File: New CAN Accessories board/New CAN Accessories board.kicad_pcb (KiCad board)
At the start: 2 copper layers, 76 parts, among them J1 39301040, J10 39301060, J2 39301040, J3 39301040, J4 39301040, J5 39301040, J6 39301040, J7 39301040, J8 39301040, J9 39301060, Q1 IRLML6344TRPBF, Q2 IRLML6344TRPBF, Q3 IRLML6344TRPBF, Q4 IRLML6344TRPBF, Q5 IRLML6344TRPBF, Q6 IRLML6344TRPBF, Q7 IRLML6344TRPBF, Q8 IRLML6344TRPBF, SW1 SW_DPDT_x2, SW3 SW_DPDT_x2, U1 NUCLEO_L432KC, U2 MCP2562FD-E_SN

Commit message: preliminary layout complete
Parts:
- removed C1, C2: 100nF, Capacitor_SMD:C_0805_2012Metric
- removed F11: Fuse, footprint:3586KTR
- removed R1, R11, R13, R15, R3, R5, R7, R9: 100, Resistor_SMD:R_0805_2012Metric
- removed R10, R12, R14, R16, R2, R26, R27, R4, R6, R8: 10K, Resistor_SMD:R_0805_2012Metric
- removed R17, R18, R19, R20, R21, R22, R23, R24: 0.05, Resistor_SMD:R_2512_6332Metric_Pad1.40x3.35mm_HandSolder
- removed R25: 120, Resistor_SMD:R_0805_2012Metric
- removed SW1, SW3: SW_DPDT_x2, footprint:SWITCH_011CQN
- removed U2: MCP2562FD-E_SN, footprint:MCP2562FD-E_SN
- added Cop1: 100nF, Capacitor_SMD:C_0805_2012Metric, B.Cu at (27.1, 40.9)
- added Cop2: 100nF, Capacitor_SMD:C_0805_2012Metric, B.Cu at (38.4, 40.9)
- added Cop3: 100nF, Capacitor_SMD:C_0805_2012Metric, B.Cu at (49.7, 40.9)
- added Cop4: 100nF, Capacitor_SMD:C_0805_2012Metric, B.Cu at (61.1, 40.9)
- added Cop5: 100nF, Capacitor_SMD:C_0805_2012Metric, B.Cu at (72.4, 40.9)
- added Cop6: 100nF, Capacitor_SMD:C_0805_2012Metric, B.Cu at (83.8, 40.9)
- added Cop7: 100nF, Capacitor_SMD:C_0805_2012Metric, B.Cu at (95.1, 40.9)
- added Cop8: 100nF, Capacitor_SMD:C_0805_2012Metric, B.Cu at (106.5, 40.9)
- added Ctr1: 100nF, Capacitor_SMD:C_0805_2012Metric, B.Cu at (76.2, 75.3)
- added Ctr2: 100nF, Capacitor_SMD:C_0805_2012Metric, B.Cu at (65.7, 77.6)
- added F8: Fuse, footprint:3586KTR, F.Cu at (105.4, 47.0)
- added J11: ATF13-2P-BM03, footprint:ATF132PBM03, F.Cu at (51.7, 68.5)
- added Rled1: 100, Resistor_SMD:R_0805_2012Metric, F.Cu at (22.9, 56.8)
- added Rled2: 100, Resistor_SMD:R_0805_2012Metric, F.Cu at (34.3, 56.8)
- added Rled3: 100, Resistor_SMD:R_0805_2012Metric, F.Cu at (45.6, 56.8)
- added Rled4: 100, Resistor_SMD:R_0805_2012Metric, F.Cu at (56.9, 56.8)
- added Rled5: 100, Resistor_SMD:R_0805_2012Metric, F.Cu at (68.3, 56.8)
- added Rled6: 100, Resistor_SMD:R_0805_2012Metric, F.Cu at (79.6, 56.8)
- added Rled7: 100, Resistor_SMD:R_0805_2012Metric, F.Cu at (91.0, 56.8)
- added Rled8: 100, Resistor_SMD:R_0805_2012Metric, F.Cu at (102.3, 56.8)
- added Rpd1: 10K, Resistor_SMD:R_0805_2012Metric, F.Cu at (21.6, 53.9)
- added Rpd2: 10K, Resistor_SMD:R_0805_2012Metric, F.Cu at (32.9, 53.9)
- added Rpd3: 10K, Resistor_SMD:R_0805_2012Metric, F.Cu at (44.3, 53.9)
- added Rpd4: 10K, Resistor_SMD:R_0805_2012Metric, F.Cu at (55.6, 53.9)
- added Rpd5: 10K, Resistor_SMD:R_0805_2012Metric, F.Cu at (67.0, 53.9)
- added Rpd6: 10K, Resistor_SMD:R_0805_2012Metric, F.Cu at (78.3, 53.9)
- added Rpd7: 10K, Resistor_SMD:R_0805_2012Metric, F.Cu at (89.7, 53.9)
- added Rpd8: 10K, Resistor_SMD:R_0805_2012Metric, F.Cu at (101.0, 53.9)
- added Rpd9: 10K, Resistor_SMD:R_0805_2012Metric, B.Cu at (69.3, 83.3)
- added Rsh1: 0.05, Resistor_SMD:R_2512_6332Metric_Pad1.40x3.35mm_HandSolder, B.Cu at (22.3, 44.6)
- added Rsh2: 0.05, Resistor_SMD:R_2512_6332Metric_Pad1.40x3.35mm_HandSolder, B.Cu at (33.7, 44.6)
- added Rsh3: 0.05, Resistor_SMD:R_2512_6332Metric_Pad1.40x3.35mm_HandSolder, B.Cu at (45.0, 44.6)
- added Rsh4: 0.05, Resistor_SMD:R_2512_6332Metric_Pad1.40x3.35mm_HandSolder, B.Cu at (56.4, 44.6)
- added Rsh5: 0.05, Resistor_SMD:R_2512_6332Metric_Pad1.40x3.35mm_HandSolder, B.Cu at (67.7, 44.6)
- added Rsh6: 0.05, Resistor_SMD:R_2512_6332Metric_Pad1.40x3.35mm_HandSolder, B.Cu at (79.0, 44.6)
- added Rsh7: 0.05, Resistor_SMD:R_2512_6332Metric_Pad1.40x3.35mm_HandSolder, B.Cu at (90.4, 44.6)
- added Rsh8: 0.05, Resistor_SMD:R_2512_6332Metric_Pad1.40x3.35mm_HandSolder, B.Cu at (101.7, 44.6)
- added Rterm1: 120, Resistor_SMD:R_0805_2012Metric, B.Cu at (29.0, 88.4)
- added SWsel1: SW_DPDT_x2, footprint:SWITCH_011CQN, F.Cu at (72.7, 85.7)
- added T1: MCP2562FD-E_SN, footprint:MCP2562FD-E_SN, B.Cu at (70.5, 74.7)
- J10: value 39301060 -> 39301040; footprint Connector_Molex:Molex_Mini-Fit_Jr_5569-06A2_2x03_P4.20mm_Horizontal -> Connector_Molex:Molex_Mini-Fit_Jr_5569-04A2_2x02_P4.20mm_Horizontal
- JP4, OP1, OP2, OP3, OP4, OP5, OP6, OP7, OP8: moved to B.Cu
- moved JP4 141.3 mm to (33.0, 89.3)
- moved D1 128.8 mm to (20.6, 56.7), turned to 90 degrees
- moved D2 119.2 mm to (32.0, 56.7), turned to 90 degrees
- moved OP1 117.6 mm to (27.1, 44.6), turned to 90 degrees
- moved J10 114.7 mm to (33.0, 84.3), turned to 90 degrees
- moved OP2 110.4 mm to (38.4, 44.6), turned to 90 degrees
- moved D3 110.1 mm to (43.3, 56.7), turned to 90 degrees
- moved OP3 104.1 mm to (49.7, 44.6), turned to 90 degrees
- moved Q1 103.5 mm to (25.7, 56.8), turned to 90 degrees
- moved D4 101.5 mm to (54.7, 56.7), turned to 90 degrees
- moved J9 99.9 mm to (33.0, 73.2), turned to 90 degrees
- moved OP4 99.1 mm to (61.1, 44.6), turned to 90 degrees
- moved Q2 99.0 mm to (37.1, 56.8), turned to 90 degrees
- moved OP5 95.3 mm to (72.4, 44.6), turned to 90 degrees
- moved D5 93.6 mm to (66.0, 56.7), turned to 90 degrees
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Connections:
- net /5V renamed 5V
- J10 pad 1: +12V -> /CANL
- J10 pad 2: +12V -> /CANH
- J10 pad 4: /CANL -> GND
- U1 pad PA10: unconnected-(U1-D0-PadPA10) -> /GATE8
- U1 pad PA11: /CANRX -> /STBY
- U1 pad PA8: /GATE2 -> /GATE3
- U1 pad PA9: /STBY -> /CANRX
- U1 pad PB0: /BOARD_SW -> /GATE7
- U1 pad PB1: /GATE1 -> /GATE4
- U1 pad PB3: /TELEM_SW -> /BOARD_SW
- U1 pad PB4: /GATE6 -> /GATE1
- U1 pad PB5: /GATE5 -> /GATE2
- U1 pad PB6: /GATE4 -> /GATE5
- U1 pad PB7: /GATE3 -> /GATE6
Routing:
- net 5V: track 0.00 -> 197.7 mm, vias 0 -> 3
- net +12V: track 0.00 -> 177.6 mm, vias 0 -> 1
- net /OA8: track 0.00 -> 85.4 mm, vias 0 -> 2
- net /OA1: track 0.00 -> 77.8 mm, vias 0 -> 2
- net /OA7: track 0.00 -> 72.3 mm, vias 0 -> 2
- net /OA2: track 0.00 -> 69.1 mm, vias 0 -> 2
- net /OA6: track 0.00 -> 63.5 mm, vias 0 -> 2
- net /OA3: track 0.00 -> 62.9 mm, vias 0 -> 2
- net /GATE1: track 0.00 -> 58.7 mm
- net /CANH: track 0.00 -> 54.1 mm
- net /OA4: track 0.00 -> 51.9 mm, vias 0 -> 2
- net /OA5: track 0.00 -> 51.1 mm, vias 0 -> 2
- net /GATE2: track 0.00 -> 49.9 mm
- net /CANL: track 0.00 -> 49.2 mm
- net GND: track 0.00 -> 45.4 mm, vias 0 -> 24
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- added copper zone on B.Cu, net +12V
- added copper zone on B.Cu, net GND
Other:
- board outline added: 105.1 x 85.8 mm

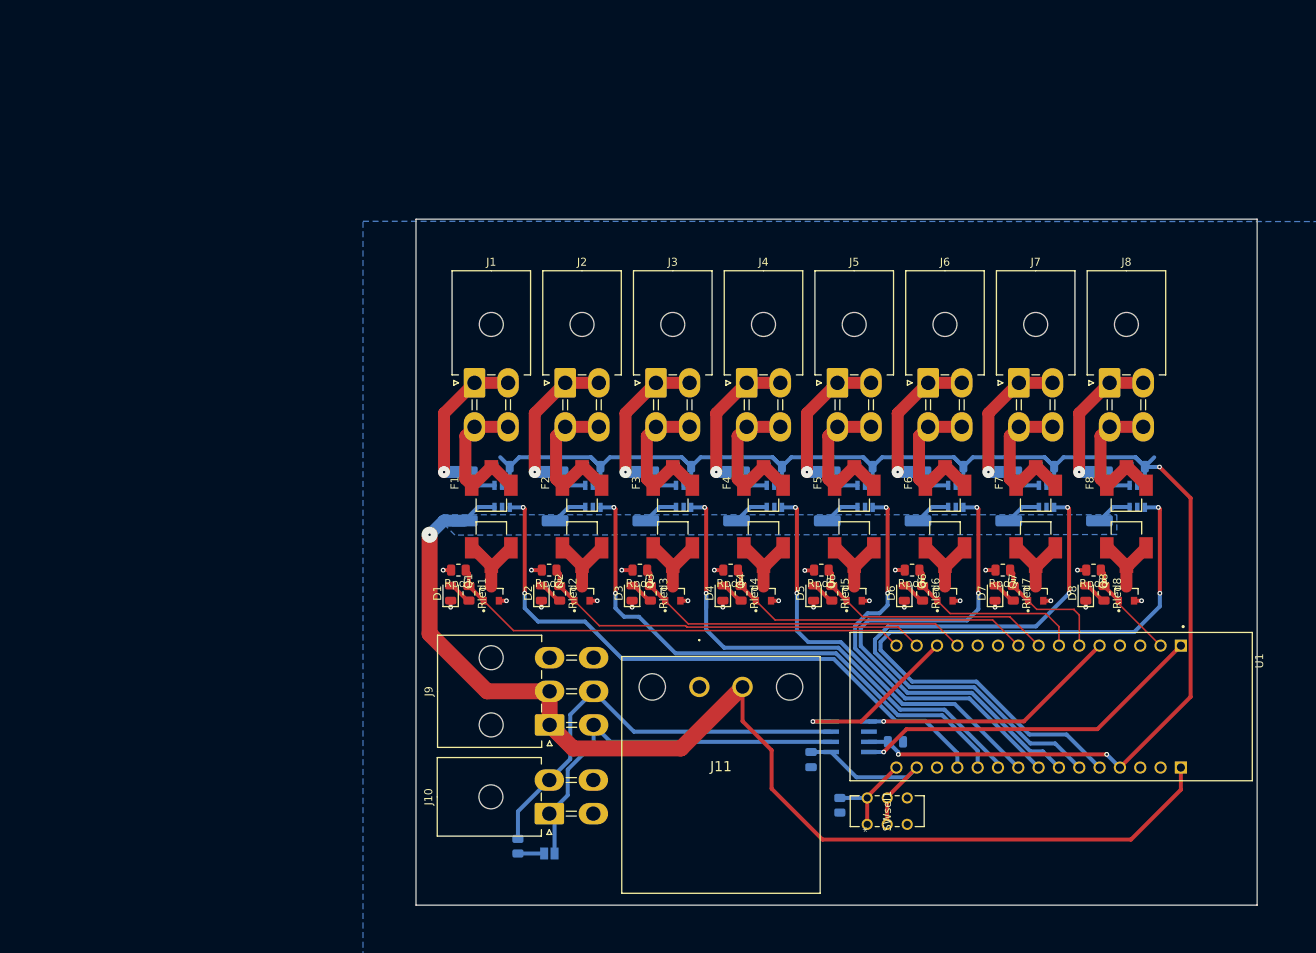
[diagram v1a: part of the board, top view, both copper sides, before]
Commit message: added test points in schematic
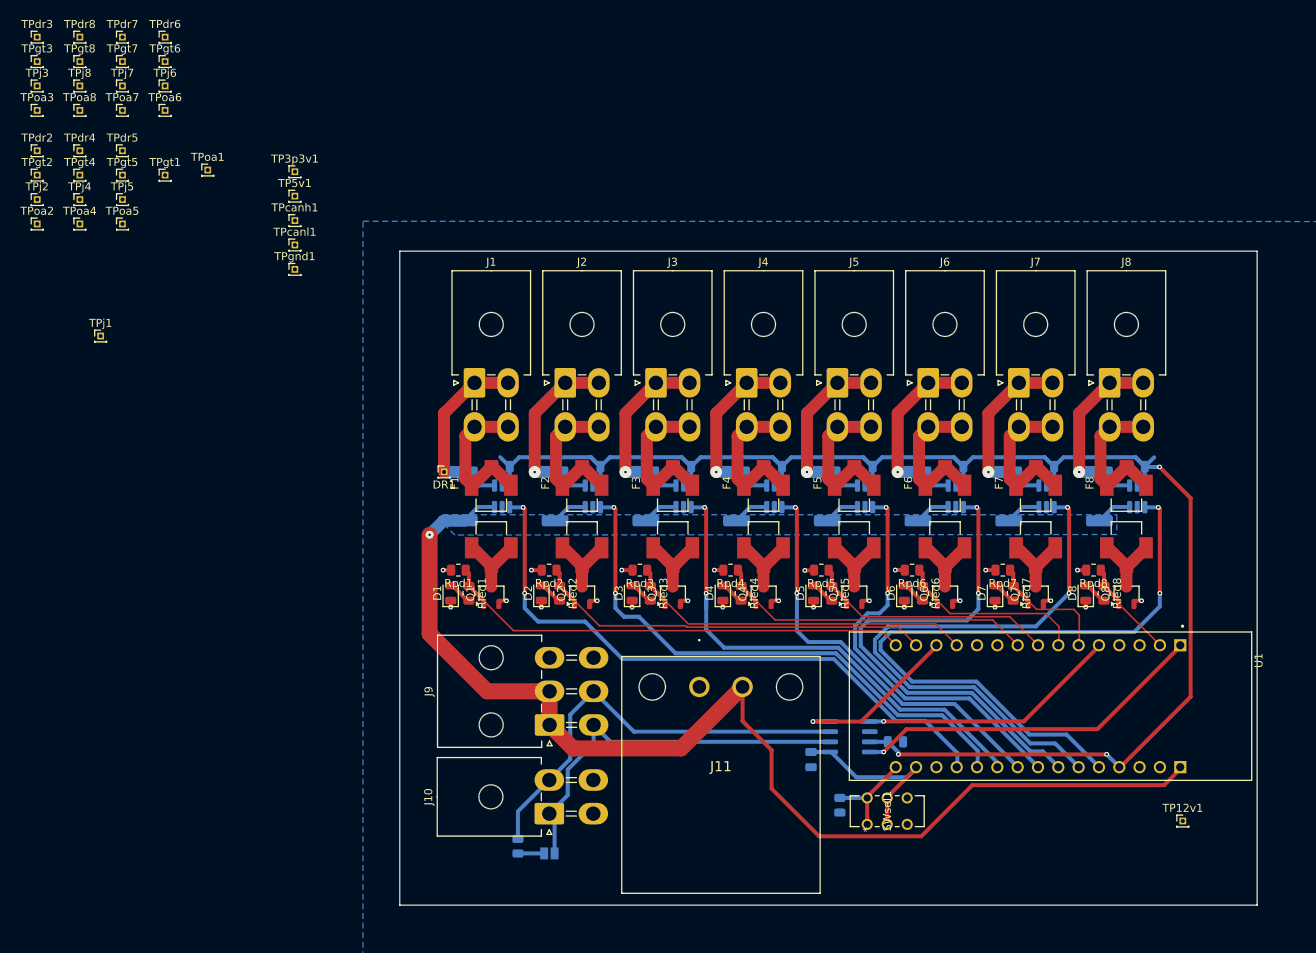
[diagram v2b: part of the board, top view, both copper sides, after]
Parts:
- added TP12v1: 12V, Connector_PinHeader_1.00mm:PinHeader_1x01_P1.00mm_Vertical, F.Cu at (112.2, 85.2)
- added TP3p3v1: 3V3, Connector_PinHeader_1.00mm:PinHeader_1x01_P1.00mm_Vertical, F.Cu at (1.17, 4.08)
- added TP5v1: 5V, Connector_PinHeader_1.00mm:PinHeader_1x01_P1.00mm_Vertical, F.Cu at (1.17, 7.12)
- added TPcanh1: CANH, Connector_PinHeader_1.00mm:PinHeader_1x01_P1.00mm_Vertical, F.Cu at (1.17, 10.2)
- added TPcanl1: CANL, Connector_PinHeader_1.00mm:PinHeader_1x01_P1.00mm_Vertical, F.Cu at (1.17, 13.2)
- added TPdr1: DR1, Connector_PinHeader_1.00mm:PinHeader_1x01_P1.00mm_Vertical, F.Cu at (19.8, 41.6)
- added TPdr2: TestPoint, Connector_PinHeader_1.00mm:PinHeader_1x01_P1.00mm_Vertical, F.Cu at (-31.1, 1.45)
- added TPdr3: TestPoint, Connector_PinHeader_1.00mm:PinHeader_1x01_P1.00mm_Vertical, F.Cu at (-31.1, -12.8)
- added TPdr4: TestPoint, Connector_PinHeader_1.00mm:PinHeader_1x01_P1.00mm_Vertical, F.Cu at (-25.7, 1.45)
- added TPdr5: TestPoint, Connector_PinHeader_1.00mm:PinHeader_1x01_P1.00mm_Vertical, F.Cu at (-20.4, 1.45)
- added TPdr6: TestPoint, Connector_PinHeader_1.00mm:PinHeader_1x01_P1.00mm_Vertical, F.Cu at (-15.1, -12.8)
- added TPdr7: TestPoint, Connector_PinHeader_1.00mm:PinHeader_1x01_P1.00mm_Vertical, F.Cu at (-20.4, -12.8)
- added TPdr8: TestPoint, Connector_PinHeader_1.00mm:PinHeader_1x01_P1.00mm_Vertical, F.Cu at (-25.7, -12.8)
- added TPgnd1: GND, Connector_PinHeader_1.00mm:PinHeader_1x01_P1.00mm_Vertical, F.Cu at (1.17, 16.3)
- added TPgt1: TestPoint, Connector_PinHeader_1.00mm:PinHeader_1x01_P1.00mm_Vertical, F.Cu at (-15.1, 4.50)
- added TPgt2: TestPoint, Connector_PinHeader_1.00mm:PinHeader_1x01_P1.00mm_Vertical, F.Cu at (-31.1, 4.50)
- added TPgt3: TestPoint, Connector_PinHeader_1.00mm:PinHeader_1x01_P1.00mm_Vertical, F.Cu at (-31.1, -9.70)
- added TPgt4: TestPoint, Connector_PinHeader_1.00mm:PinHeader_1x01_P1.00mm_Vertical, F.Cu at (-25.7, 4.50)
- added TPgt5: TestPoint, Connector_PinHeader_1.00mm:PinHeader_1x01_P1.00mm_Vertical, F.Cu at (-20.4, 4.50)
- added TPgt6: TestPoint, Connector_PinHeader_1.00mm:PinHeader_1x01_P1.00mm_Vertical, F.Cu at (-15.1, -9.70)
- added TPgt7: TestPoint, Connector_PinHeader_1.00mm:PinHeader_1x01_P1.00mm_Vertical, F.Cu at (-20.4, -9.70)
- added TPgt8: TestPoint, Connector_PinHeader_1.00mm:PinHeader_1x01_P1.00mm_Vertical, F.Cu at (-25.7, -9.70)
- added TPj1: TestPoint, Connector_PinHeader_1.00mm:PinHeader_1x01_P1.00mm_Vertical, F.Cu at (-23.1, 24.6)
- added TPj2: TestPoint, Connector_PinHeader_1.00mm:PinHeader_1x01_P1.00mm_Vertical, F.Cu at (-31.1, 7.55)
- added TPj3: TestPoint, Connector_PinHeader_1.00mm:PinHeader_1x01_P1.00mm_Vertical, F.Cu at (-31.1, -6.65)
- added TPj4: TestPoint, Connector_PinHeader_1.00mm:PinHeader_1x01_P1.00mm_Vertical, F.Cu at (-25.7, 7.55)
- added TPj5: TestPoint, Connector_PinHeader_1.00mm:PinHeader_1x01_P1.00mm_Vertical, F.Cu at (-20.4, 7.55)
- added TPj6: TestPoint, Connector_PinHeader_1.00mm:PinHeader_1x01_P1.00mm_Vertical, F.Cu at (-15.1, -6.65)
- added TPj7: TestPoint, Connector_PinHeader_1.00mm:PinHeader_1x01_P1.00mm_Vertical, F.Cu at (-20.4, -6.65)
- added TPj8: TestPoint, Connector_PinHeader_1.00mm:PinHeader_1x01_P1.00mm_Vertical, F.Cu at (-25.7, -6.65)
- added TPoa1: TestPoint, Connector_PinHeader_1.00mm:PinHeader_1x01_P1.00mm_Vertical, F.Cu at (-9.73, 3.86)
- added TPoa2: TestPoint, Connector_PinHeader_1.00mm:PinHeader_1x01_P1.00mm_Vertical, F.Cu at (-31.1, 10.6)
- added TPoa3: TestPoint, Connector_PinHeader_1.00mm:PinHeader_1x01_P1.00mm_Vertical, F.Cu at (-31.1, -3.60)
- added TPoa4: TestPoint, Connector_PinHeader_1.00mm:PinHeader_1x01_P1.00mm_Vertical, F.Cu at (-25.7, 10.6)
- added TPoa5: TestPoint, Connector_PinHeader_1.00mm:PinHeader_1x01_P1.00mm_Vertical, F.Cu at (-20.4, 10.6)
- added TPoa6: TestPoint, Connector_PinHeader_1.00mm:PinHeader_1x01_P1.00mm_Vertical, F.Cu at (-15.1, -3.60)
- added TPoa7: TestPoint, Connector_PinHeader_1.00mm:PinHeader_1x01_P1.00mm_Vertical, F.Cu at (-20.4, -3.60)
- added TPoa8: TestPoint, Connector_PinHeader_1.00mm:PinHeader_1x01_P1.00mm_Vertical, F.Cu at (-25.7, -3.60)
- J1, J2, J3, J4, J5, J6, J7, J8: footprint Connector_Molex:Molex_Mini-Fit_Jr_5569-04A2_2x02_P4.20mm_Horizontal -> footprint:Molex_Mini-Fit_Jr_5569-04A2_2x02_P4.20mm_Horizontal
- OP1, OP2, OP3, OP4, OP5, OP6, OP7, OP8: value MCP6C02T-020E/CHY -> MCP6C02T-020; footprint footprint:SOT-23-6_CHY_MCH-M -> Package_TO_SOT_SMD:SOT-23-6_Handsoldering
- Q1, Q2, Q3, Q4, Q5, Q6, Q7, Q8: footprint footprint:TRANS_IRLML6344TRPBF -> Package_TO_SOT_SMD:TSOT-23
- T1: footprint footprint:MCP2562FD-E_SN -> Package_SO:SOIC-8_3.9x4.9mm_P1.27mm
- moved U1 0.09 mm to (95.6, 70.9)
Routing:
- net +12V: track 177.6 -> 175.7 mm
- net Net-(J1-Pin_1): vias 1 -> 0
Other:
- board size 105.1 x 85.8 mm -> 107.2 x 81.8 mm

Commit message: post design review
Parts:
- added H1: MountingHole, MountingHole:MountingHole_3.2mm_M3_ISO14580, F.Cu at (119.0, 19.0)
- added H2: MountingHole, MountingHole:MountingHole_3.2mm_M3_ISO14580, F.Cu at (119.0, 95.0)
- added H3: MountingHole, MountingHole:MountingHole_3.2mm_M3_ISO14580, F.Cu at (19.0, 95.0)
- TPdr1: value DR1 -> TestPoint
- moved TPoa8 147.7 mm to (109.1, 56.8)
- moved TPgt8 147.4 mm to (104.2, 60.0)
- moved TPdr8 141.6 mm to (100.6, 51.1)
- moved TPgnd1 134.7 mm to (116.9, 85.2)
- moved TPj8 133.9 mm to (99.2, 41.6)
- moved TPgt7 132.9 mm to (92.8, 60.0)
- moved TPoa7 132.7 mm to (97.7, 56.8)
- moved TP5v1 129.3 mm to (104.2, 85.2)
- moved TPdr7 126.9 mm to (89.3, 51.1)
- moved TPj7 118.5 mm to (87.9, 41.6)
- moved TPoa6 118.1 mm to (86.4, 56.8)
- moved TPgt6 117.2 mm to (79.5, 59.5)
- moved TP3p3v1 113.4 mm to (75.2, 89.9)
- moved TPdr6 112.8 mm to (78.0, 51.1)
- moved TPgt5 106.2 mm to (70.1, 60.0)
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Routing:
- net +12V: track 175.7 -> 184.5 mm
- net /CANH: track 54.1 -> 60.9 mm
- net /3V3: track 23.7 -> 27.9 mm
- net 5V: track 197.7 -> 201.1 mm
- net /CANL: track 49.2 -> 52.5 mm
- net /OA6: track 63.5 -> 61.3 mm, vias 2 -> 1
- net Net-(F7-Pad2): track 9.35 -> 11.4 mm
- net Net-(F4-Pad2): track 9.35 -> 11.4 mm
- net Net-(F3-Pad2): track 9.35 -> 11.4 mm
- net Net-(F2-Pad2): track 9.35 -> 11.4 mm
- net Net-(F1-Pad2): track 9.35 -> 11.4 mm
- net Net-(F8-Pad2): track 9.35 -> 11.4 mm
- net Net-(F6-Pad2): track 9.35 -> 11.4 mm
- net Net-(F5-Pad2): track 9.35 -> 11.4 mm
- net /OA3: track 62.9 -> 61.0 mm, vias 2 -> 1
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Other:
- board size 107.2 x 81.8 mm -> 110 x 86 mm

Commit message: Added test points 1x12 pin and 1x8 pin
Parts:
- removed JP4: SolderJumper_2_Open, Jumper:SolderJumper-2_P1.3mm_Open_Pad1.0x1.5mm
- removed TP12v1: 12V, Connector_PinHeader_1.00mm:PinHeader_1x01_P1.00mm_Vertical
- removed TP3p3v1: 3V3, Connector_PinHeader_1.00mm:PinHeader_1x01_P1.00mm_Vertical
- removed TP5v1: 5V, Connector_PinHeader_1.00mm:PinHeader_1x01_P1.00mm_Vertical
- removed TPgnd1: GND, Connector_PinHeader_1.00mm:PinHeader_1x01_P1.00mm_Vertical
- removed TPgt2, TPgt3, TPgt4, TPgt5, TPgt6, TPgt7, TPgt8, TPoa1, TPoa2, TPoa3, TPoa4, TPoa5, TPoa6, TPoa7, TPoa8: TestPoint, Connector_PinHeader_1.00mm:PinHeader_1x01_P1.00mm_Vertical
- added J12: Conn_01x02_Pin, Connector_PinHeader_2.54mm:PinHeader_1x02_P2.54mm_Vertical, F.Cu at (29.2, 97.3)
- added J13: Conn_01x12_Pin, Connector_PinHeader_2.54mm:PinHeader_1x12_P2.54mm_Vertical, F.Cu at (81.5, 93.0)
- added J14: Conn_01x08_Pin, Connector_PinHeader_2.54mm:PinHeader_1x08_P2.54mm_Vertical, F.Cu at (80.0, 65.0)
- added JP1: SolderJumper_2_Open, Jumper:SolderJumper-2_P1.3mm_Open_Pad1.0x1.5mm, B.Cu at (32.9, 89.4)
- moved Ctr2 11.2 mm to (59.9, 87.2)
- moved Ctr1 11.2 mm to (70.5, 85.0)
- moved T1 11.2 mm to (64.8, 84.3)
- moved Rpd9 9.36 mm to (65.8, 91.9)
- moved SWsel1 8.73 mm to (71.4, 94.3)
- moved U1 8.19 mm to (94.5, 79.0)
- moved J11 0.20 mm to (51.9, 68.5)
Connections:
- net +12V renamed 12V
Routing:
- net /3V3: track 27.9 -> 52.0 mm
- net /OA8: track 85.4 -> 105.7 mm, vias 1 -> 2
- net /OA7: track 72.2 -> 91.9 mm, vias 1 -> 2
- net /OA6: track 61.3 -> 79.5 mm, vias 1 -> 2
- net /OA5: track 51.1 -> 68.9 mm, vias 1 -> 2
- net /OA2: track 69.1 -> 85.0 mm, vias 1 -> 2
- net /OA1: track 79.0 -> 94.2 mm, vias 1 -> 2
- net /OA3: track 61.0 -> 76.1 mm, vias 1 -> 2
- net /OA4: track 51.9 -> 66.8 mm, vias 1 -> 2
- net 5V: track 201.1 -> 215.0 mm
- net /GATE8: track 14.4 -> 28.3 mm
- net /GATE1: track 60.5 -> 73.4 mm
- net /GATE2: track 51.7 -> 62.6 mm
- net /CANRX: track 44.4 -> 52.2 mm
- net /GATE3: track 45.5 -> 52.8 mm
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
